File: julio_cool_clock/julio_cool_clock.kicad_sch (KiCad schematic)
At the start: 26 parts, among them J1 PJ-102AH, J2 Conn_01x06, J2 PJ-102AH, U1 ATmega328-PU, U2 L7805, Y1 Crystal_16MHz

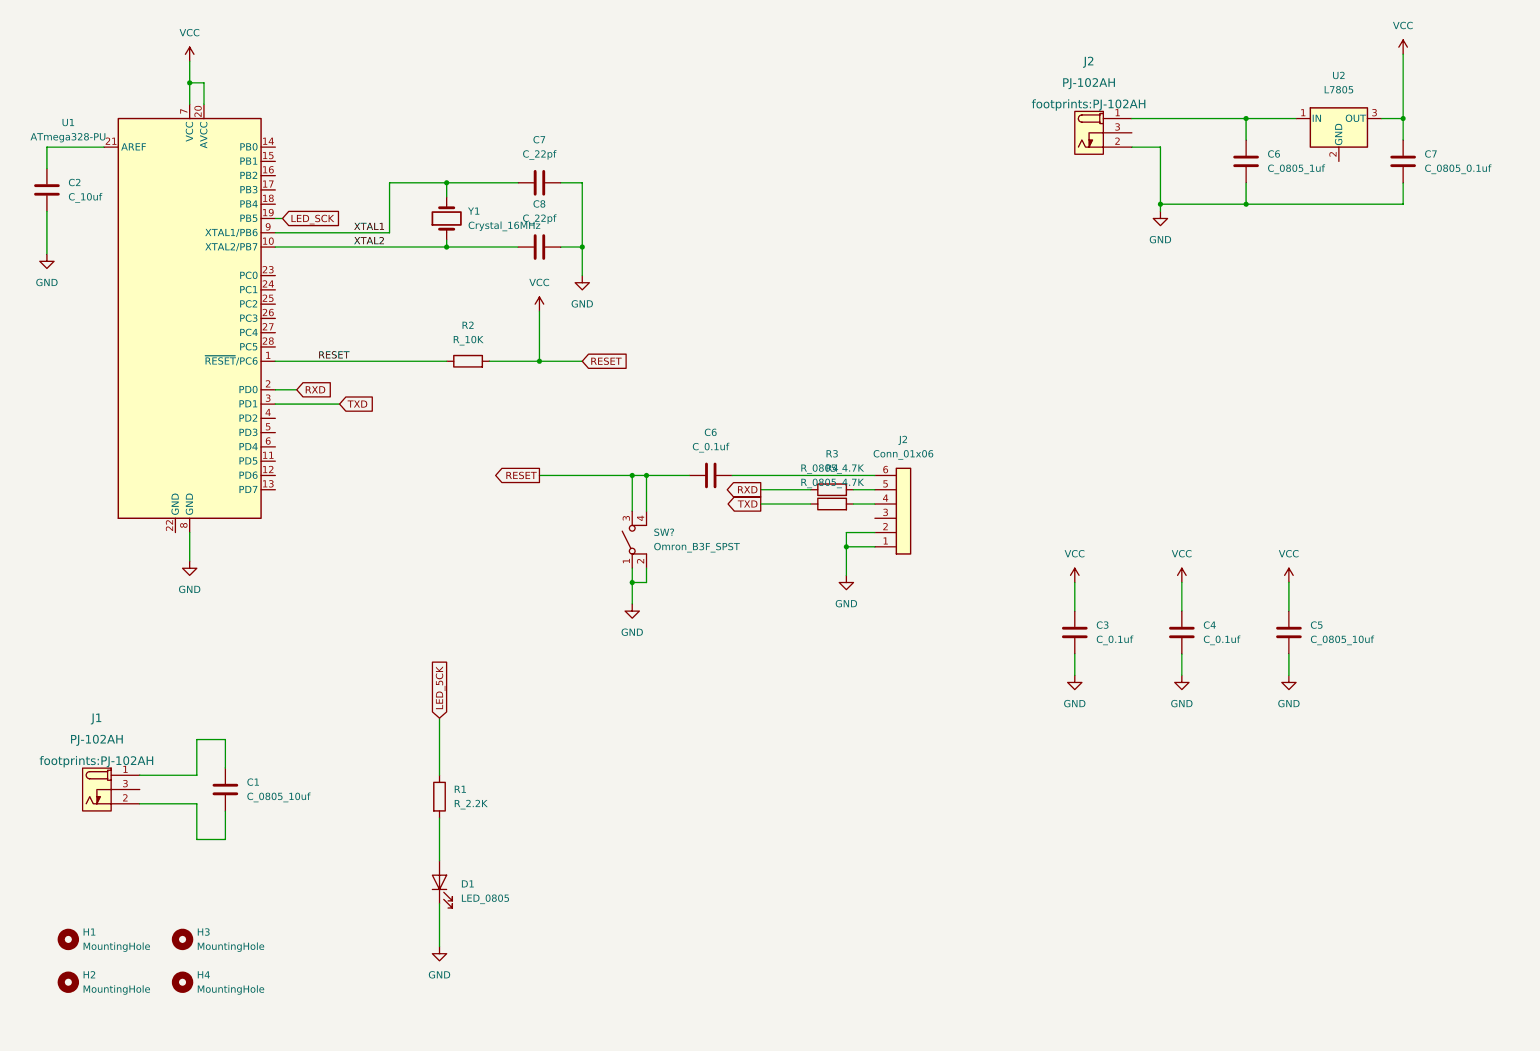
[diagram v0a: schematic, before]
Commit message: Design Commit 3
Cleaned up the existing components and added inputs + outputs to the schematic as well.
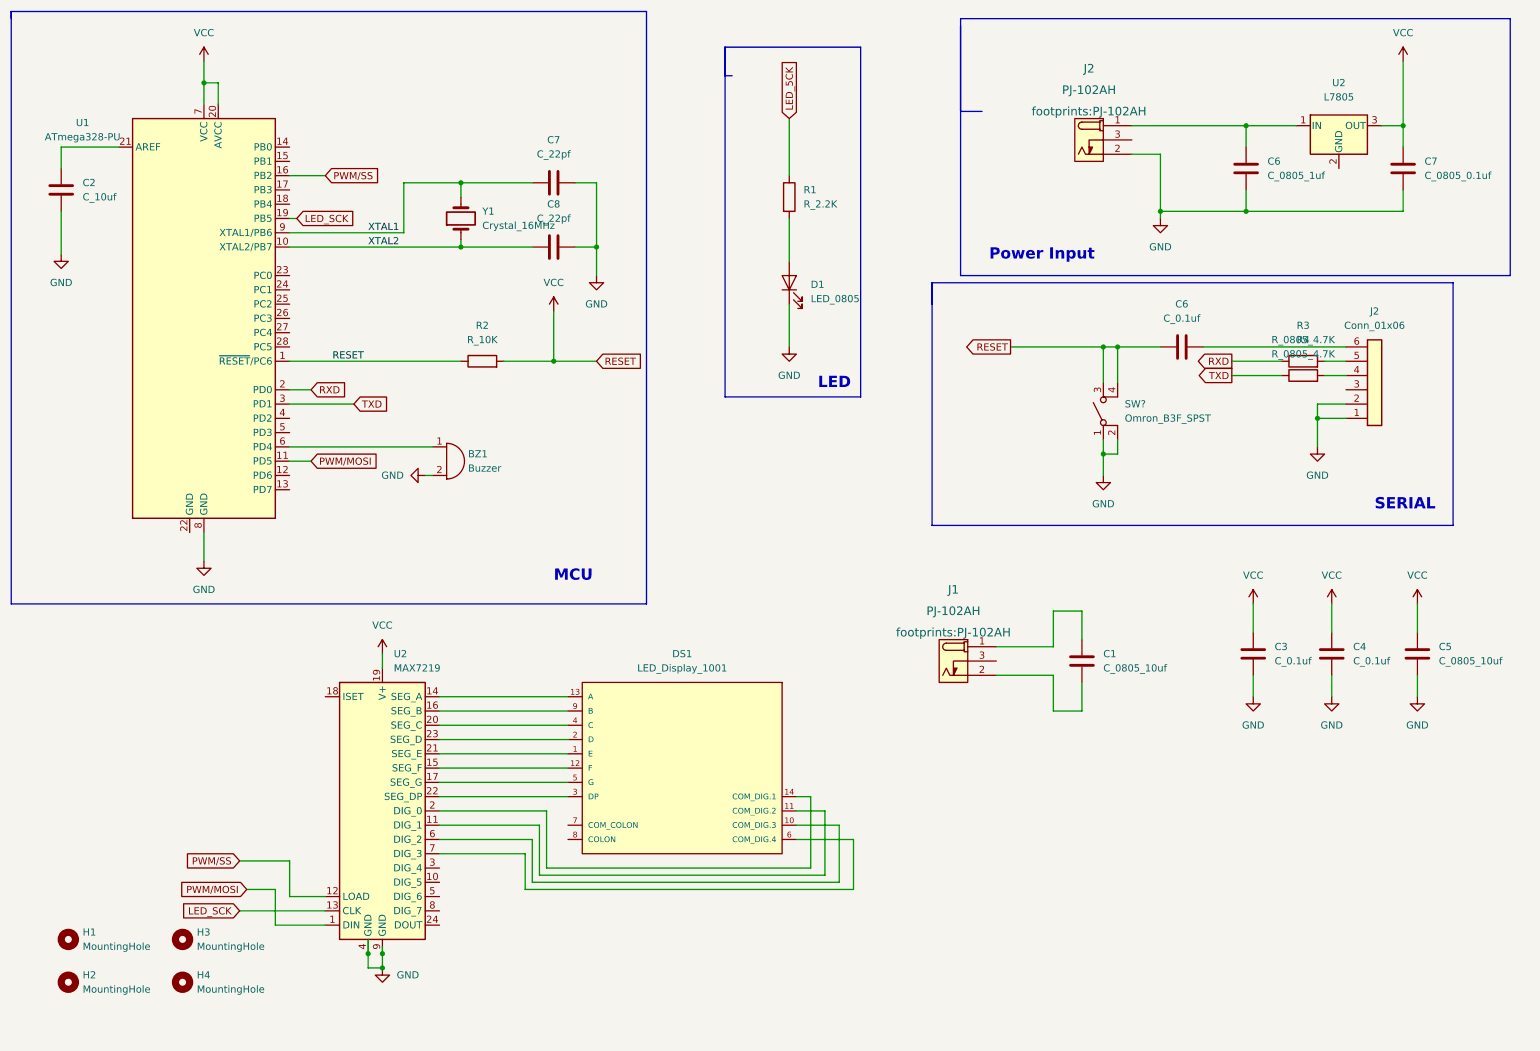
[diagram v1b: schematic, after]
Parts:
- added BZ1: Buzzer, footprints:Buzzer_TDK_PS1240P02BT_D12.2mm_H6.5mm, symbol HPS:Buzzer
- added DS1: LED_Display_1001, footprints:Adafruit-1001-0-0-MFG, symbol HPS:LED_Display_1001
- added U2: MAX7219, footprints:DIP-24_W7.62mm, symbol HPS:MAX7219
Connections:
- net GND: now also BZ1.2 (+), U2.4 (GND), U2.9 (GND)
- net LED_SCK: now also U2.13 (CLK)
- net VCC: now also U2.19 (V+)
- net PWM/MOSI: now reaches U1.11 (PD5)
- net PWM/MOSI: now also U2.1 (DIN)
- net PWM/SS: now reaches U1.16 (PB2)
- net PWM/SS: now also U2.12 (LOAD)
- net at U1.6 (PD4): now also BZ1.1 (-)
- new net: DS1.1 (E), U2.21 (SEG_E)
- new net: DS1.10 (COM_DIG.3), U2.6 (DIG_2)
- new net: DS1.11 (COM_DIG.2), U2.11 (DIG_1)
- new net: DS1.12 (F), U2.15 (SEG_F)
- new net: DS1.13 (A), U2.14 (SEG_A)
- new net: DS1.14 (COM_DIG.1), U2.2 (DIG_0)
- new net: DS1.2 (D), U2.23 (SEG_D)
- new net: DS1.3 (DP), U2.22 (SEG_DP)
- new net: DS1.4 (C), U2.20 (SEG_C)
- new net: DS1.5 (G), U2.17 (SEG_G)
- new net: DS1.6 (COM_DIG.4), U2.7 (DIG_3)
- new net: DS1.9 (B), U2.16 (SEG_B)
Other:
- note added: "LED"
- note added: "MCU"
- note added: "Power Input"
- note added: "SERIAL"
- moved on the sheet: C1, C2, C3, C4, C5, C6, C7, C8, D1, J1, J2, R1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

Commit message: Design Commit 4
I refined the schematic and added the RTC, buttons, and the LCD display for my clock.
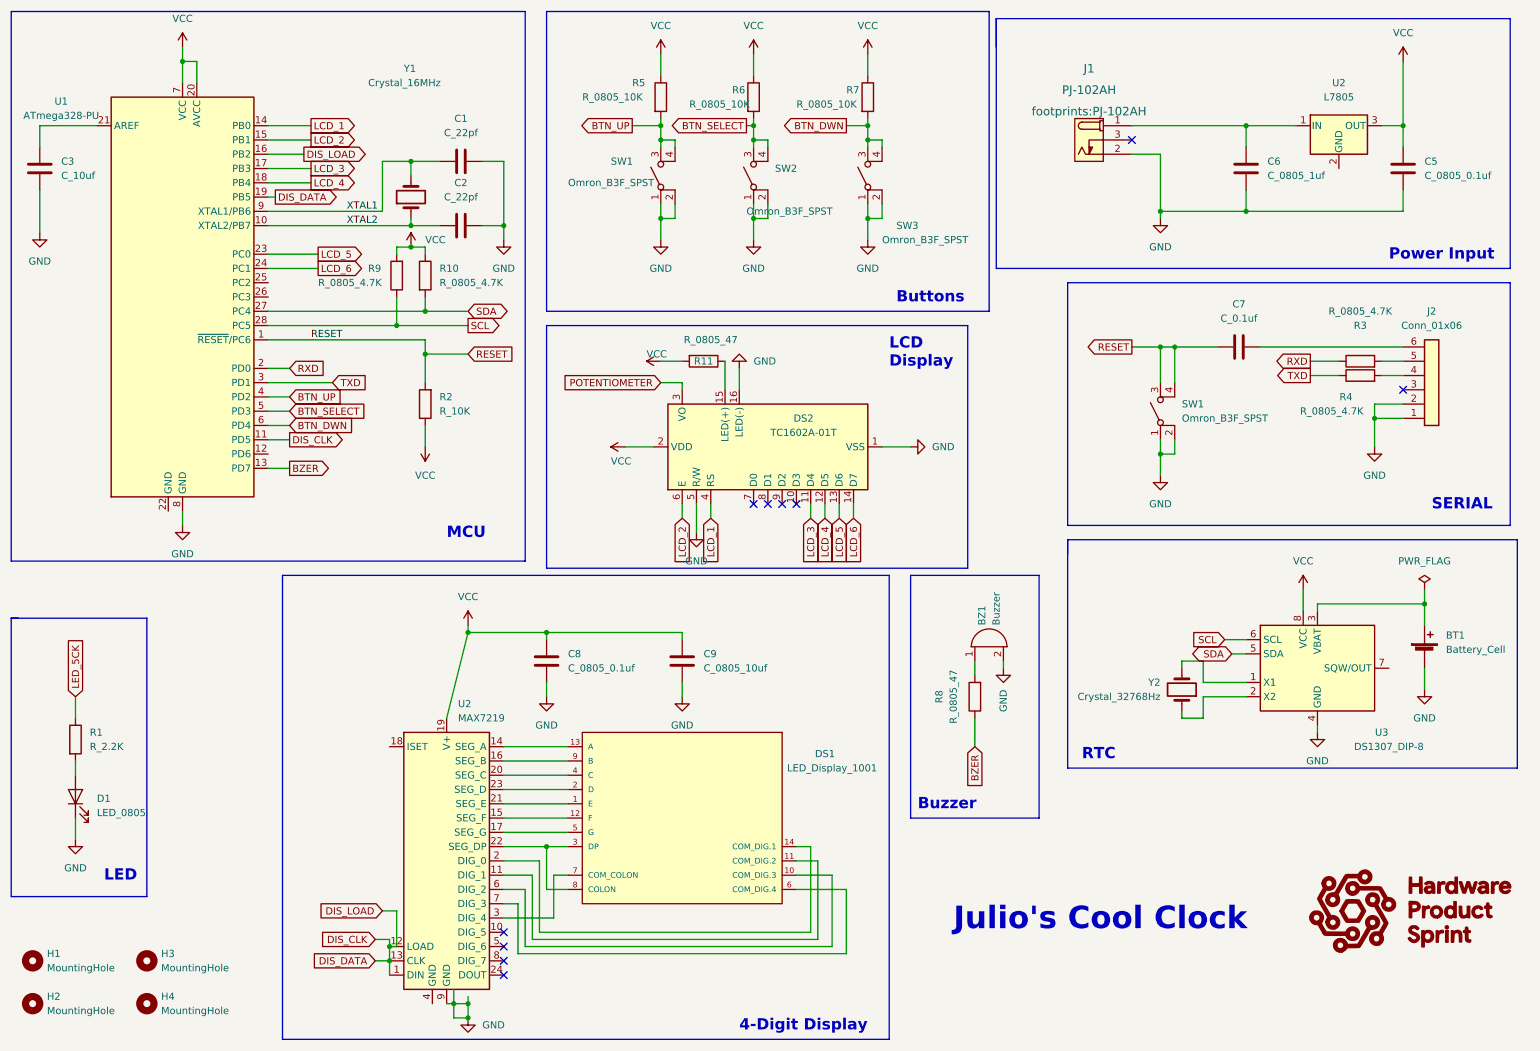
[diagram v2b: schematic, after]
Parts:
- removed C1, C5: C_0805_10uf, footprints:C_0805_2012Metric, symbol HPS:C_0805_10uf
- removed C3, C4: C_0.1uf, footprints:C_0805_2012Metric, symbol HPS:C_0805_0.1uf
- removed J1: PJ-102AH, footprints:PJ-102AH, symbol HPS:PJ-102AH
- added BT1: Battery_Cell, footprints:BatteryHolder_Keystone_106_1x20mm, symbol HPS:Battery_Cell
- added C8: C_0805_0.1uf, footprints:C_0805_2012Metric, symbol HPS:C_0805_0.1uf
- added C9: C_0805_10uf, footprints:C_0805_2012Metric, symbol HPS:C_0805_10uf
- added DS2: TC1602A-01T, footprints:TC1602A-01T, symbol HPS:TC1602A-01T
- added R10, R9: R_0805_4.7K, footprints:R_0805_2012Metric, symbol HPS:R_0805_4.7K
- added R11, R8: R_0805_47, footprints:R_0805_2012Metric, symbol HPS:R_0805_47
- added R5, R6, R7: R_0805_10K, footprints:R_0805_2012Metric, symbol HPS:R_0805_10K
- added SW1, SW2, SW3: Omron_B3F_SPST, footprints:SW_SPST_Omron_B3FS-100xP, symbol HPS:Omron_B3F_SPST
- added U3: DS1307_DIP-8, footprints:DIP-8_W7.62mm, symbol HPS:DS1307_DIP-8
- added Y2: Crystal_32768Hz, footprints:Crystal_SMD_2Pin_3.2x1.5mm, symbol HPS:Crystal_32768Hz
- gave numbers to parts that had none: 1
- renumbered C7 to C1, C8 to C2, C2 to C3, C7 to C5, C6 to C7, J2 to J1
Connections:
- net PWM/MOSI is gone; now on net DIS_CLK: U1.11 (PD5), U2.1 (DIN)
- net PWM/SS is gone; now on net DIS_CLK: U1.16 (PB2), U2.12 (LOAD)
- net GND: now also BT1.2 (-), C8.2, C9.2, DS2.1 (VSS), DS2.16 (LED(-)), DS2.5 (R/W), SW1.1 (A), SW1.2 (A), SW2.1 (A), SW2.2 (A), SW3.1 (A), SW3.2 (A), U3.4 (GND); no longer U2.4 (GND)
- net VCC: now also C8.1, C9.1, DS2.2 (VDD), R10.1, R11.2, R5.1, R6.1, R7.1, R9.2, U3.8 (VCC); no longer C7.1, R2.2, SW1.3 (B), SW1.4 (B), U1.1 (~{RESET}/PC6)
- net at BZ1.1 (-): now also R8.2; no longer U1.6 (PD4)
- net at DS1.3 (DP), U2.22 (SEG_DP): now also DS1.8 (COLON)
- net at DS1.7 (COM_COLON): now also U2.3 (DIG_4)
- net BZER: now reaches U1.13 (PD7)
- net BZER: now also R8.1
- net LCD_1: now reaches U1.14 (PB0)
- net LCD_1: now also DS2.4 (RS)
- net LCD_2: now reaches U1.15 (PB1)
- net LCD_2: now also DS2.6 (E)
- net LCD_3: now reaches U1.17 (PB3)
- net LCD_3: now also DS2.11 (D4)
- net LCD_4: now reaches U1.18 (PB4)
- net LCD_4: now also DS2.12 (D5)
- net LCD_5: now reaches U1.23 (PC0)
- net LCD_5: now also DS2.13 (D6)
- net LCD_6: now reaches U1.24 (PC1)
- net LCD_6: now also DS2.14 (D7)
- net SDA: now reaches U1.27 (PC4)
- net SDA: now also R10.2, U3.5 (SDA)
- net SCL: now reaches U1.28 (PC5)
- net SCL: now also R9.1, U3.6 (SCL)
- net BTN_UP: now reaches U1.4 (PD2)
- net BTN_UP: now also R5.2, SW1.3 (B), SW1.4 (B)
- net BTN_SELECT: now reaches U1.5 (PD3)
- net BTN_SELECT: now also R6.2, SW2.3 (B), SW2.4 (B)
- net LED_SCK renamed DIS_CLK
- new net: U3.2 (X2), Y2.1
- new net: U3.1 (X1), Y2.2
- new net: BT1.1 (+), U3.3 (VBAT)
- new net: DS2.15 (LED(+)), R11.1
- new net BTN_DWN: R7.2, SW3.3 (B), SW3.4 (B), U1.6 (PD4)
- new net POTENTIOMETER: DS2.3 (VO)
- new net RESET: C7.1, R2.2, SW1.3 (B), SW1.4 (B), U1.1 (~{RESET}/PC6)
- no-connect marks 0 -> 10
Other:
- note added: "4-Digit Display"
- note added: "Buttons"
- note added: "Buzzer"
- note added: "Julio's Cool Clock"
- note added: "LCD Display"
- note added: "RTC"
- moved on the sheet: BZ1, C1, C2, C3, C7, D1, DS1, H1, H2, H3, H4, J2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

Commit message: Design Commit 4.1
Fixed some wiring that was undone.
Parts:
- renumbered C3 to C1, C1 to C2, C2 to C3, C8 to C4, C9 to C5, C7 to C6, C6 to C7, C5 to C8, DS2 to DS1, DS1 to DS2, R3 to R10, R4 to R11, R9 to R2, R10 to R3, R2 to R4, R11 to R6, R6 to R7, R7 to R8, R8 to R9, SW1 to SW4, U2 to U4
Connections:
- net DIS_CLK: no longer U1.16 (PB2), U1.19 (PB5), U2.1 (DIN), U2.12 (LOAD)
- net GND: now also U2.4 (GND)
- new net DIS_DATA: U1.19 (PB5), U2.1 (DIN)
- new net DIS_LOAD: U1.16 (PB2), U2.12 (LOAD)
